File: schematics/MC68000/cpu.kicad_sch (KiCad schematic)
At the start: 58 parts, among them J2 Conn_02x37_Row_Letter_Last, SW1 Reset, U1 74LS00, U10 74LS244, U11 74LS244, U12 74LS148, U2 74LS05, U3 74LS161, U4 ICM7555xB, U5 68000D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

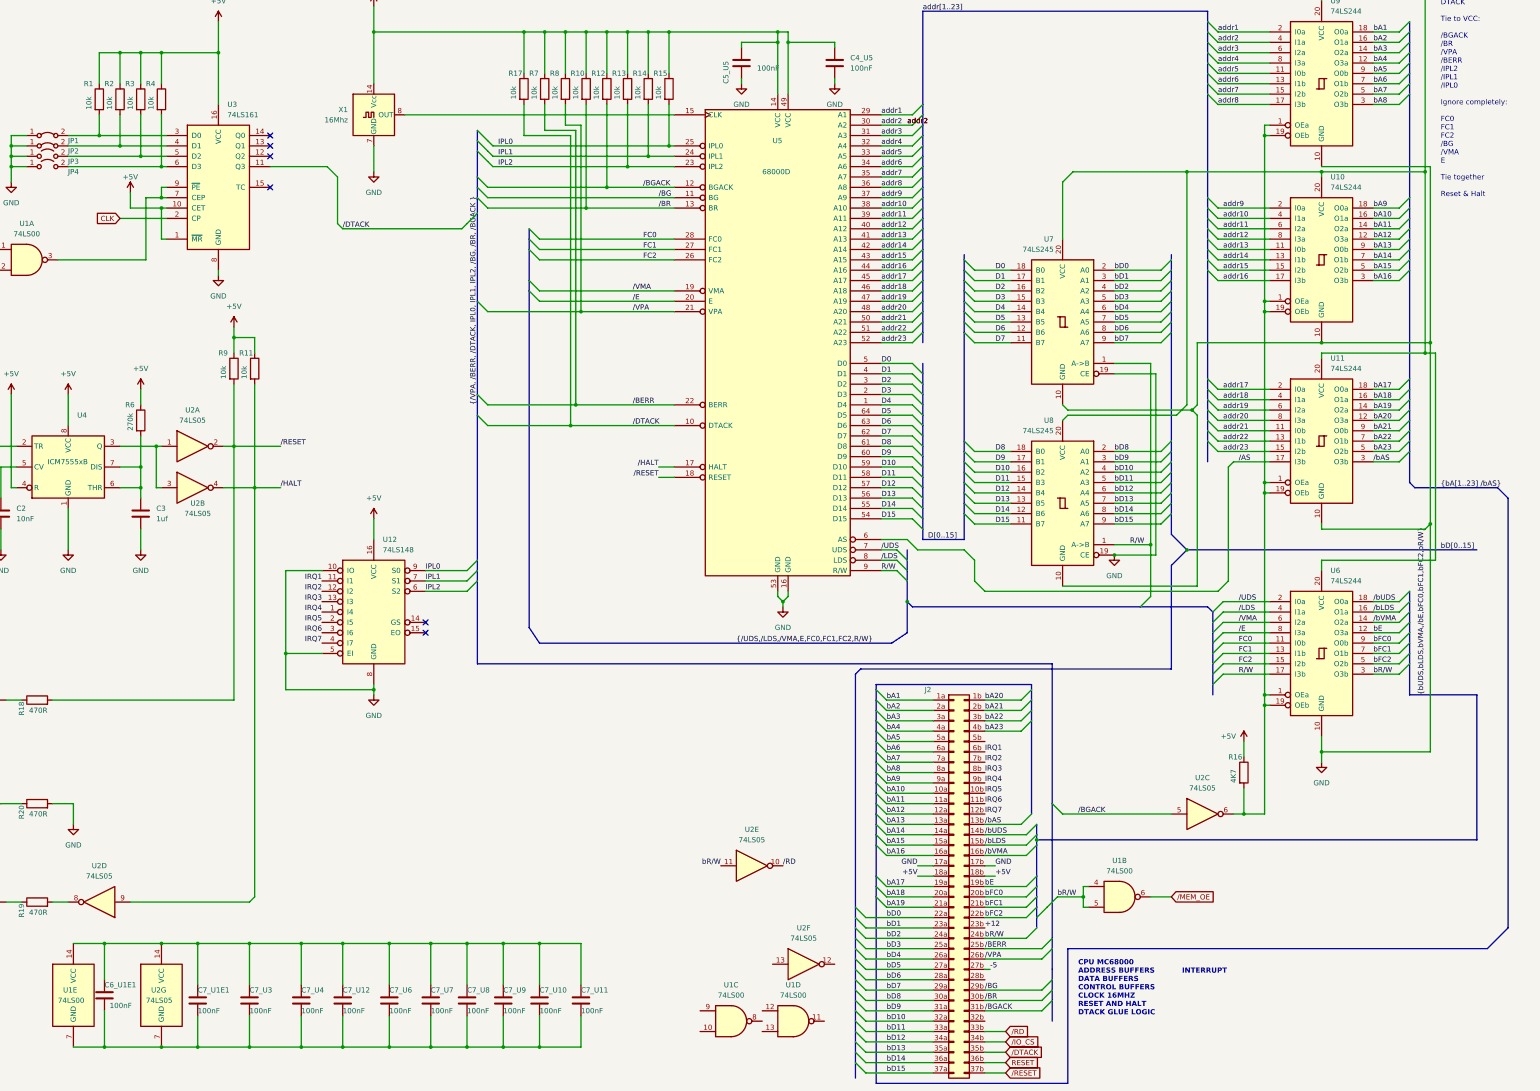
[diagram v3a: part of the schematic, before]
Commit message: Uart reading writing with counter.asm
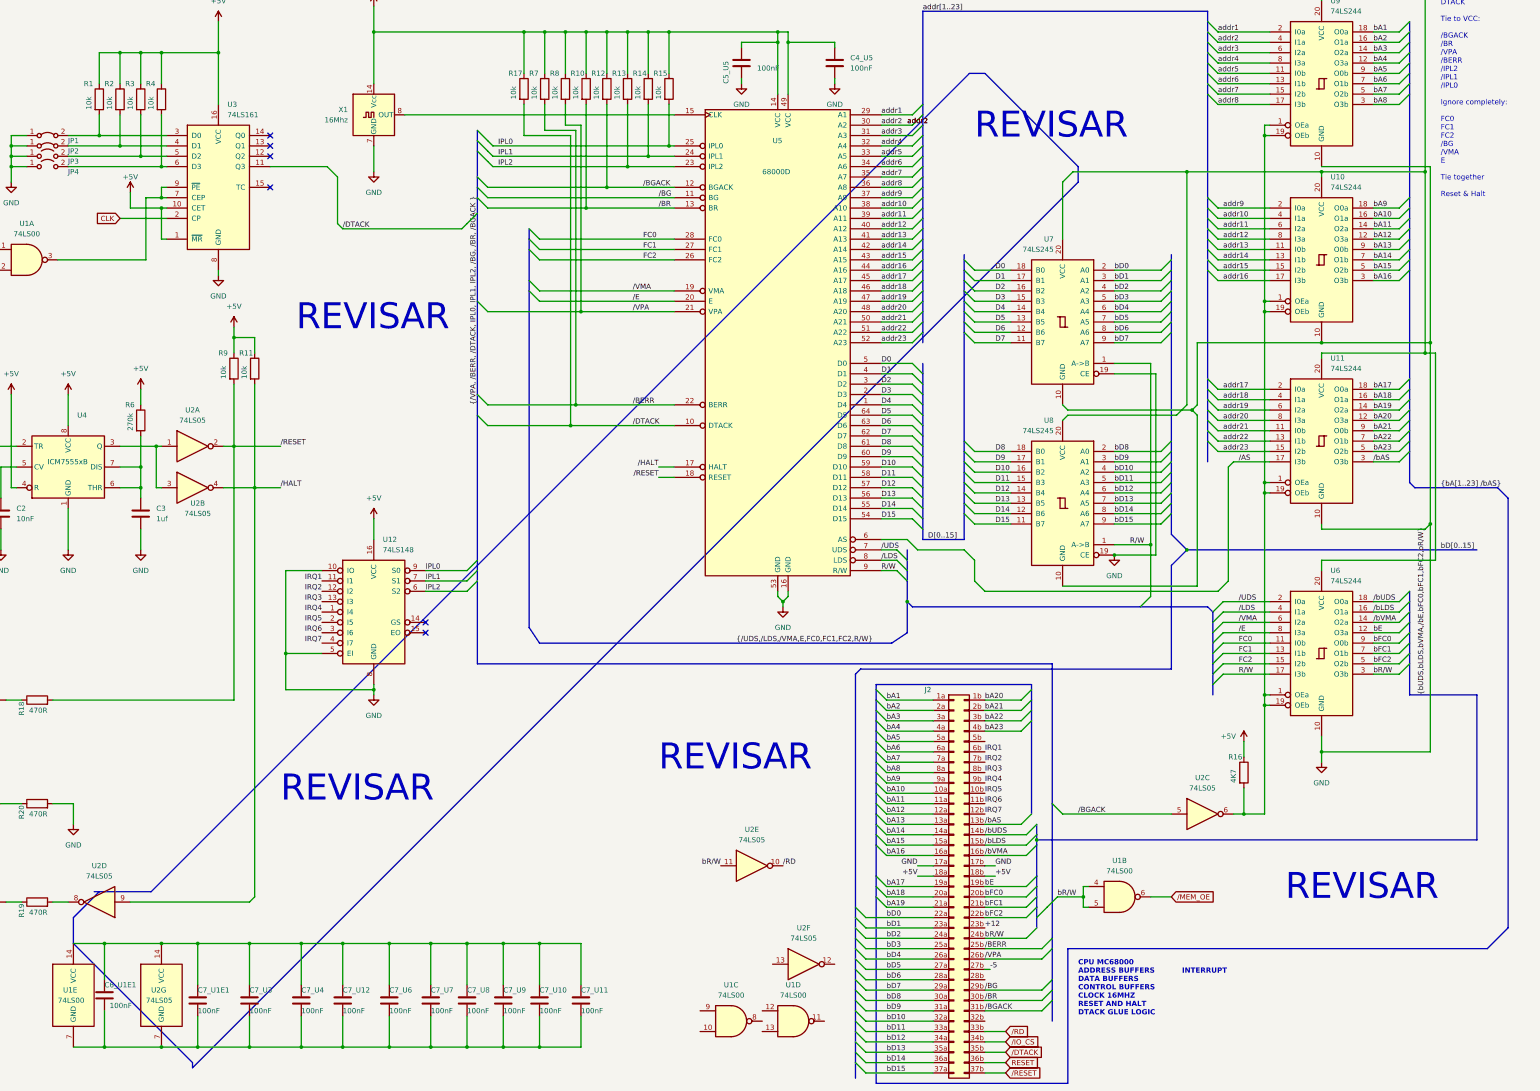
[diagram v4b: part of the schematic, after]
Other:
- note added: "REVISAR"
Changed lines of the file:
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@@
+    (stroke (width 0) (type default))
+  )
+  (polyline (pts (xy 59.69 237.49) (xy 73.66 237.49))
     (stroke (width 0) (type default))
   )
@@
     (stroke (width 0) (type default))
   )
+  (polyline (pts (xy 54.61 243.84) (xy 60.96 237.49))
+    (stroke (width 0) (type default))
+  )
   (wire (pts (xy 180.34 44.45) (xy 180.34 69.85))
     (stroke (width 0) (type default))
@@
     (stroke (width 0) (type default))
   )
+  (polyline (pts (xy 83.82 279.4) (xy 54.61 250.19))
+    (stroke (width 0) (type default))
+  )
   (bus (pts (xy 332.74 85.09) (xy 332.74 111.76))
     (stroke (width 0) (type default))
@@
     (stroke (width 0) (type default))
   )
-  (bus (pts (xy 294.64 256.54) (xy 294.64 259.08))
+  (bus (pts (xy 294.64 251.46) (xy 294.64 259.08))
     (stroke (width 0) (type default))
   )
@@
     (stroke (width 0) (type default))
   )
+  (polyline (pts (xy 300.99 59.69) (xy 300.99 63.5))
+    (stroke (width 0) (type default))
+  )
   (wire (pts (xy 254 195.58) (xy 265.43 195.58))
     (stroke (width 0) (type default))
@@
     (stroke (width 0) (type default))
   )
-  (bus (pts (xy 294.64 251.46) (xy 294.64 256.54))
-    (stroke (width 0) (type default))
-  )
   (bus (pts (xy 382.27 176.53) (xy 382.27 179.07))
     (stroke (width 0) (type default))
@@
     (stroke (width 0) (type default))
   )
+  (polyline (pts (xy 300.99 63.5) (xy 83.82 280.67))
+    (stroke (width 0) (type default))
+  )
   (bus (pts (xy 382.27 77.47) (xy 382.27 80.01))
     (stroke (width 0) (type default))
@@
     (stroke (width 0) (type default))
   )
+  (polyline (pts (xy 73.66 237.49) (xy 274.32 36.83))
+    (stroke (width 0) (type default))
+  )
   (wire (pts (xy 278.13 231.14) (xy 280.67 231.14))
     (stroke (width 0) (type default))
@@
     (stroke (width 0) (type default))
   )
+  (polyline (pts (xy 274.32 36.83) (xy 278.13 36.83))
+    (stroke (width 0) (type default))
+  )
   (wire (pts (xy 156.21 55.88) (xy 157.48 57.15))
     (stroke (width 0) (type default))
@@
     (stroke (width 0) (type default))
   )
+  (polyline (pts (xy 54.61 250.19) (xy 54.61 243.84))
+    (stroke (width 0) (type default))
+  )
   (wire (pts (xy 228.6 166.37) (xy 229.87 165.1))
     (stroke (width 0) (type default))
@@
     (stroke (width 0) (type default))
   )
+  (polyline (pts (xy 83.82 280.67) (xy 83.82 279.4))
+    (stroke (width 0) (type default))
+  )
   (wire (pts (xy 373.38 44.45) (xy 379.73 44.45))
     (stroke (width 0) (type default))
@@
   )
   (bus (pts (xy 294.64 248.92) (xy 294.64 251.46))
+    (stroke (width 0) (type default))
+  )
+  (polyline (pts (xy 278.13 36.83) (xy 300.99 59.69))
     (stroke (width 0) (type default))
   )
@@
     (effects (font (size 1.27 1.27) (thickness 0.254) bold) (justify left bottom))
   )
+  (text "REVISAR" (at 105.41 215.9 0)
+    (effects (font (size 6.35 6.35)) (justify left bottom))
+  )
+  (text "REVISAR" (at 351.79 240.03 0)
+    (effects (font (size 6.35 6.35)) (justify left bottom))
+  )
   (text "PARA FINS DE TESTE\nNO LUGAR DE /ROM_CE\nE /RAM_CS ESTOU \nUSANDO O SINAL \nDA CPU /AS "
     (at 12.7 77.47 0)
@@
     (effects (font (size 1.27 1.27)) (justify left bottom))
   )
+  (text "REVISAR" (at 275.59 53.34 0)
+    (effects (font (size 6.35 6.35)) (justify left bottom))
+  )
+  (text "REVISAR" (at 198.12 208.28 0)
+    (effects (font (size 6.35 6.35)) (justify left bottom))
+  )
+  (text "REVISAR" (at 109.22 100.33 0)
+    (effects (font (size 6.35 6.35)) (justify left bottom))
+  )
   (label "bD9" (at 254 266.7 0) (fields_autoplaced)

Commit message: Compilando com linker
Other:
- note added: "nao estou usando o chip que pode provocar wait states nesse momento DTACK está sendo tratado na GAL"
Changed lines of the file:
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@@
     (effects (font (size 6.35 6.35)) (justify left bottom))
+  )
+  (text "nao estou usando o chip que \npode provocar wait states\nnesse momento DTACK está \nsendo tratado na GAL"
+    (at 53.34 95.25 0)
+    (effects (font (size 1.27 1.27)) (justify left bottom))
   )
   (text "REVISAR" (at 109.22 100.33 0)
